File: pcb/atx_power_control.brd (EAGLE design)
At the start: 86 x 70 mm, 65 parts, among them IC2 REG1117, IC3 STM32F042F4, IC4 MY_7905DT, J1 ATX24RH, SW1 324_SW, SW2 324_SW, SW3 324_SW, SW4 324_SW, SW5 324_SW, SW7 324_SW, U1 USBC_16P, U2 USBC_16P

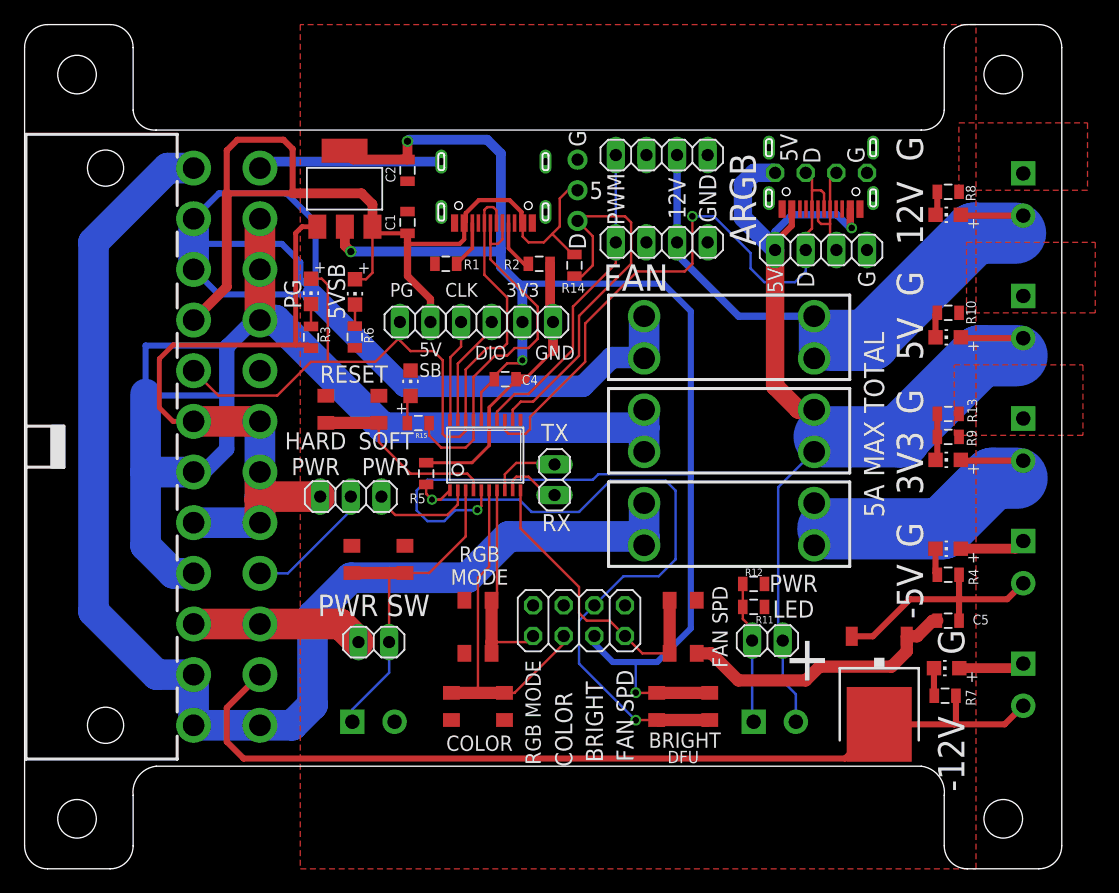
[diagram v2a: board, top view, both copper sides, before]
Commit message: adjusted LED resistor value, optimised GND plane
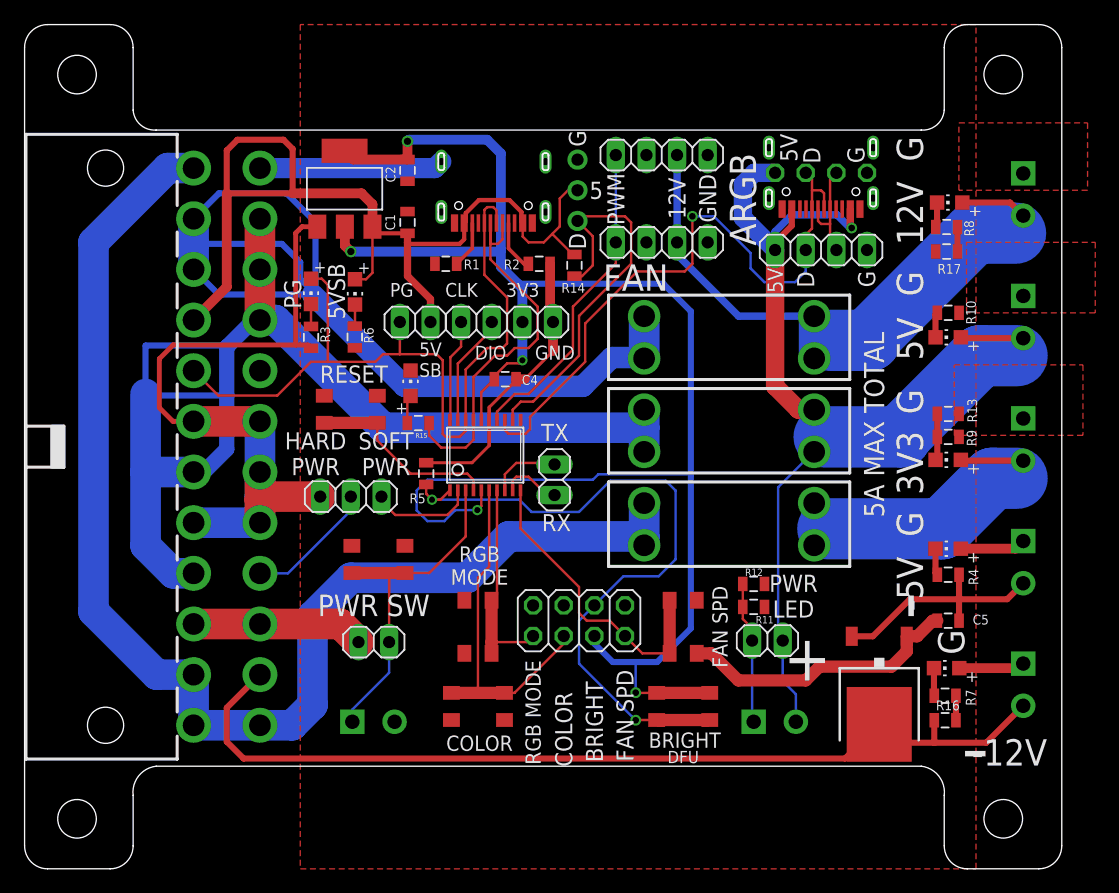
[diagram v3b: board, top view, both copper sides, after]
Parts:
- added R16, R17: 5K, SparkFun-Passives:0805
- moved R8 2.92 mm to (76.5, 53.2)
- moved LED5 1.02 mm to (76.7, 55.2)
- moved SW3 0.13 mm to (27.1, 38.1)
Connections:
- new net N$28: R16.2, R7.1
- new net N$32: R17.2, R8.1
- net GND: now also R17.1; no longer R8.1
- net N$2: now also R16.1; no longer R7.1
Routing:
- net N$32: track 0.00 -> 2.03 mm
- net N$28: track 0.00 -> 2.03 mm
- net N$2: track 77.6 -> 78.3 mm
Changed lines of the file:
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@@
 <board>
 <plain>
-<text x="73.406" y="22.987" size="2.1844" layer="25" rot="R90" align="center">-5V</text>
+<text x="73.406" y="23.622" size="2.1844" layer="25" rot="R90" align="center">-5V</text>
 <text x="73.406" y="33.655" size="2.1844" layer="25" rot="R90" align="center">3V3</text>
-<text x="76.835" y="9.525" size="2.1844" layer="25" rot="R90" align="center">-12V</text>
+<text x="81.661" y="9.652" size="2.1844" layer="25" rot="R180" align="center">-12V</text>
 <text x="73.406" y="43.942" size="2.1844" layer="25" rot="R90" align="center">5V</text>
 <text x="73.406" y="54.356" size="2.1844" layer="25" rot="R90" align="center">12V</text>
@@
 <text x="73.406" y="48.514" size="2.1844" layer="25" rot="R270" align="center">G</text>
 <text x="73.406" y="38.735" size="2.1844" layer="25" rot="R270" align="center">G</text>
-<text x="73.406" y="27.686" size="2.1844" layer="25" rot="R270" align="center">G</text>
+<text x="73.406" y="28.575" size="2.1844" layer="25" rot="R270" align="center">G</text>
 <text x="76.835" y="18.796" size="2.1844" layer="25" rot="R270" align="center">G</text>
 <text x="33.655" y="42.2102" size="1.143" layer="25" rot="R180" align="center">5V
@@
 <text x="45.8424" y="52.0408" size="1.4224" layer="25" rot="R270" align="center">D</text>
 <text x="47.4002" y="56.2564" size="1.4224" layer="25" align="center">5</text>
+<rectangle x1="77.978" y1="9.3218" x2="79.6798" y2="9.779" layer="25"/>
+<rectangle x1="72.6567" y1="21.5773" x2="74.3585" y2="22.0345" layer="25" rot="R90"/>
 </plain>
 <attributes>
@@
 <attribute name="NAME" x="42.5706" y="40.9413" size="0.8128" layer="25" rot="R180"/>
 </element>
-<element name="SW3" library="3pos_slide_switch_centered" package="342_SWICH_FOOT" value="324_SW" x="27.178" y="38.1" smashed="yes" rot="R180"/>
+<element name="SW3" library="3pos_slide_switch_centered" package="342_SWICH_FOOT" value="324_SW" x="27.051" y="38.1" smashed="yes" rot="R180"/>
 <element name="SW4" library="3pos_slide_switch_centered" package="342_SWICH_FOOT" value="324_SW" x="54.61" y="13.462" smashed="yes" rot="R180"/>
 <element name="LED1" library="adafruit" package="CHIP-LED0805" value="" x="76.581" y="26.543" smashed="yes" rot="R90">
@@
 <attribute name="NAME" x="78.0415" y="14.859" size="0.8128" layer="25" rot="R270"/>
 </element>
-<element name="LED5" library="adafruit" package="CHIP-LED0805" value="" x="76.581" y="54.229" smashed="yes" rot="R90">
-<attribute name="VALUE" x="77.851" y="56.769" size="1.27" layer="27" rot="R180"/>
-</element>
-<element name="R8" library="SparkFun-Passives" package="0805" value="5K" x="76.581" y="56.134" smashed="yes" rot="R180">
-<attribute name="NAME" x="78.0415" y="56.6928" size="0.8128" layer="25" rot="R270"/>
+<element name="LED5" library="adafruit" package="CHIP-LED0805" value="" x="76.708" y="55.245" smashed="yes" rot="R90">
+<attribute name="VALUE" x="77.978" y="57.785" size="1.27" layer="27" rot="R180"/>
+</element>
+<element name="R8" library="SparkFun-Passives" package="0805" value="5K" x="76.454" y="53.213" smashed="yes" rot="R180">
+<attribute name="NAME" x="77.9145" y="53.7718" size="0.8128" layer="25" rot="R270"/>
 </element>
 <element name="LED6" library="adafruit" package="CHIP-LED0805" value="" x="76.581" y="33.909" smashed="yes" rot="R90">
@@
 <element name="LED8" library="adafruit" package="CHIP-LED0805" value="" x="32.004" y="40.259" smashed="yes">
 <attribute name="VALUE" x="34.544" y="38.989" size="1.27" layer="27" rot="R90"/>
+</element>
+<element name="R16" library="SparkFun-Passives" package="0805" value="5K" x="76.327" y="12.319" smashed="yes">
+<attribute name="NAME" x="75.565" y="13.1445" size="0.8128" layer="25"/>
+</element>
+<element name="R17" library="SparkFun-Passives" package="0805" value="5K" x="76.454" y="51.181" smashed="yes">
+<attribute name="NAME" x="75.692" y="49.3395" size="0.8128" layer="25"/>
 </element>
 </elements>
@@
 <contactref element="LED1" pad="A"/>
 <contactref element="LED4" pad="A"/>
-<contactref element="R8" pad="1"/>
 <contactref element="R9" pad="1"/>
 <contactref element="R10" pad="1"/>
@@
 <contactref element="JP2" pad="4"/>
 <contactref element="JP7" pad="4"/>
-<wire x1="34.556" y1="58.6395" x2="20.0535" y2="58.6395" width="0.8128" layer="16"/>
-<wire x1="20.0535" y1="58.6395" x2="19.514" y2="58.1" width="0.8128" layer="16"/>
 <contactref element="JP6" pad="1"/>
 <contactref element="J5" pad="2"/>
@@
 <contactref element="JP11" pad="3"/>
 <contactref element="LED8" pad="C"/>
+<contactref element="R17" pad="1"/>
+<wire x1="34.556" y1="58.6395" x2="34.0165" y2="58.1" width="1.6764" layer="16"/>
+<wire x1="34.0165" y1="58.1" x2="19.514" y2="58.1" width="1.6764" layer="16"/>
 </signal>
 <signal name="+3V3">
@@
 <wire x1="37.221" y1="32.248" x2="37.221" y2="31.3862" width="0.2032" layer="1"/>
 <wire x1="37.221" y1="32.248" x2="36.703" y2="32.766" width="0.2032" layer="1"/>
-<wire x1="29.378" y1="36.975" x2="24.978" y2="36.975" width="1.016" layer="1"/>
+<wire x1="29.251" y1="36.975" x2="24.851" y2="36.975" width="1.016" layer="1"/>
 <wire x1="36.703" y1="32.766" x2="32.004" y2="32.766" width="0.2032" layer="1"/>
-<wire x1="29.378" y1="36.975" x2="29.378" y2="35.392" width="0.2032" layer="1"/>
-<wire x1="29.378" y1="35.392" x2="32.004" y2="32.766" width="0.2032" layer="1"/>
+<wire x1="29.251" y1="36.975" x2="29.251" y2="35.519" width="0.2032" layer="1"/>
+<wire x1="29.251" y1="35.519" x2="32.004" y2="32.766" width="0.2032" layer="1"/>
 </signal>
 <signal name="BUTTON2">
@@
 <contactref element="IC4" pad="3"/>
 <contactref element="J1" pad="14"/>
-<contactref element="R7" pad="1"/>
 <contactref element="J3" pad="2"/>
 <wire x1="68.032" y1="9.144" x2="70.866" y2="11.978" width="0.508" layer="1"/>
@@
 <wire x1="16.764" y1="10.541" x2="18.161" y2="9.144" width="0.508" layer="1"/>
 <wire x1="18.161" y1="9.144" x2="68.032" y2="9.144" width="0.508" layer="1"/>
-<wire x1="70.866" y1="11.978" x2="77.089" y2="11.978" width="0.508" layer="1"/>
-<wire x1="77.089" y1="11.978" x2="81.264" y2="11.978" width="0.508" layer="1"/>
-<wire x1="81.264" y1="11.978" x2="82.804" y2="13.518" width="0.508" layer="1"/>
-<wire x1="77.227" y1="14.351" x2="77.227" y2="12.116" width="0.508" layer="1"/>
-<wire x1="77.227" y1="12.116" x2="77.089" y2="11.978" width="0.508" layer="1"/>
+<wire x1="79.74" y1="10.454" x2="75.438" y2="10.454" width="0.508" layer="1"/>
+<wire x1="75.438" y1="10.454" x2="72.39" y2="10.454" width="0.508" layer="1"/>
+<wire x1="70.866" y1="11.978" x2="72.39" y2="10.454" width="0.508" layer="1"/>
+<wire x1="79.74" y1="10.454" x2="82.804" y2="13.518" width="0.508" layer="1"/>
+<contactref element="R16" pad="1"/>
+<wire x1="75.427" y1="12.319" x2="75.427" y2="10.465" width="0.508" layer="1"/>
+<wire x1="75.427" y1="10.465" x2="75.438" y2="10.454" width="0.508" layer="1"/>
 </signal>
 <signal name="N$11">
@@
 <contactref element="LED5" pad="C"/>
 <contactref element="R8" pad="2"/>
-<wire x1="75.681" y1="56.134" x2="75.681" y2="54.379" width="0.508" layer="1"/>
-<wire x1="75.681" y1="54.379" x2="75.531" y2="54.229" width="0.508" layer="1"/>
+<wire x1="75.658" y1="55.245" x2="75.658" y2="53.317" width="0.508" layer="1"/>
+<wire x1="75.658" y1="53.317" x2="75.554" y2="53.213" width="0.508" layer="1"/>
 </signal>
 <signal name="N$10">
@@
 <wire x1="23.749" y1="42.037" x2="20.955" y2="39.243" width="0.2032" layer="1"/>
 <wire x1="25.146" y1="42.037" x2="23.749" y2="42.037" width="0.2032" layer="1"/>
-<wire x1="31.115" y1="44.069" x2="29.083" y2="42.037" width="0.2032" layer="1"/>
-<wire x1="29.083" y1="42.037" x2="25.146" y2="42.037" width="0.2032" layer="1"/>
+<wire x1="25.146" y1="42.037" x2="29.083" y2="42.037" width="0.2032" layer="1"/>
 <wire x1="34.925" y1="35.814" x2="34.671" y2="36.068" width="0.2032" layer="1"/>
-<wire x1="34.671" y1="42.164" x2="33.909" y2="42.926" width="0.2032" layer="1"/>
-<wire x1="33.909" y1="42.926" x2="32.004" y2="42.926" width="0.2032" layer="1"/>
-<wire x1="31.115" y1="43.815" x2="31.115" y2="45.339" width="0.2032" layer="1"/>
+<wire x1="34.163" y1="42.672" x2="34.671" y2="42.164" width="0.2032" layer="1"/>
 <wire x1="34.671" y1="36.068" x2="34.671" y2="42.164" width="0.2032" layer="1"/>
-<wire x1="32.004" y1="42.926" x2="31.115" y2="43.815" width="0.2032" layer="1"/>
-<wire x1="31.115" y1="44.069" x2="31.115" y2="45.339" width="0" layer="19" extent="1-1"/>
+<wire x1="29.083" y1="42.037" x2="29.718" y2="42.672" width="0.2032" layer="1"/>
+<wire x1="29.718" y1="42.672" x2="31.115" y2="42.672" width="0.2032" layer="1"/>
+<wire x1="31.115" y1="42.672" x2="34.163" y2="42.672" width="0.2032" layer="1"/>
+<wire x1="31.115" y1="45.339" x2="31.115" y2="42.672" width="0.2032" layer="1"/>
 </signal>
 <signal name="N$30">
@@
 <contactref element="U$5" pad="B0"/>
 <contactref element="U$5" pad="B1"/>
-<wire x1="82.804" y1="54.158" x2="77.702" y2="54.158" width="0.508" layer="1"/>
-<wire x1="77.702" y1="54.158" x2="77.631" y2="54.229" width="0.508" layer="1"/>
 <wire x1="82.169" y1="52.705" x2="78.74" y2="52.705" width="5.08" layer="16"/>
 <wire x1="78.74" y1="52.705" x2="70.104" y2="44.069" width="5.08" layer="16"/>
@@
 <wire x1="66.802" y1="43.701" x2="66.802" y2="43.651" width="0.2032" layer="16"/>
 <wire x1="66.802" y1="43.651" x2="65.47" y2="42.319" width="0.2032" layer="16"/>
+<wire x1="77.758" y1="55.245" x2="81.717" y2="55.245" width="0.508" layer="1"/>
+<wire x1="81.717" y1="55.245" x2="82.804" y2="54.158" width="0.508" layer="1"/>
 </signal>
 <signal name="N$16">
@@
 <wire x1="31.739" y1="38.944" x2="31.739" y2="36.957" width="0.2032" layer="1"/>
 </signal>
+<signal name="N$28">
+<contactref element="R7" pad="1"/>
+<contactref element="R16" pad="2"/>
+<wire x1="77.227" y1="14.351" x2="77.227" y2="12.319" width="0.508" layer="1"/>
+</signal>
+<signal name="N$32">
+<contactref element="R8" pad="1"/>
+<contactref element="R17" pad="2"/>
+<wire x1="77.354" y1="53.213" x2="77.354" y2="51.181" width="0.508" layer="1"/>
+</signal>
 </signals>

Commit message: moved ARGB header, removed GND thermals, jumper pad on USBC data lines, finishing touches
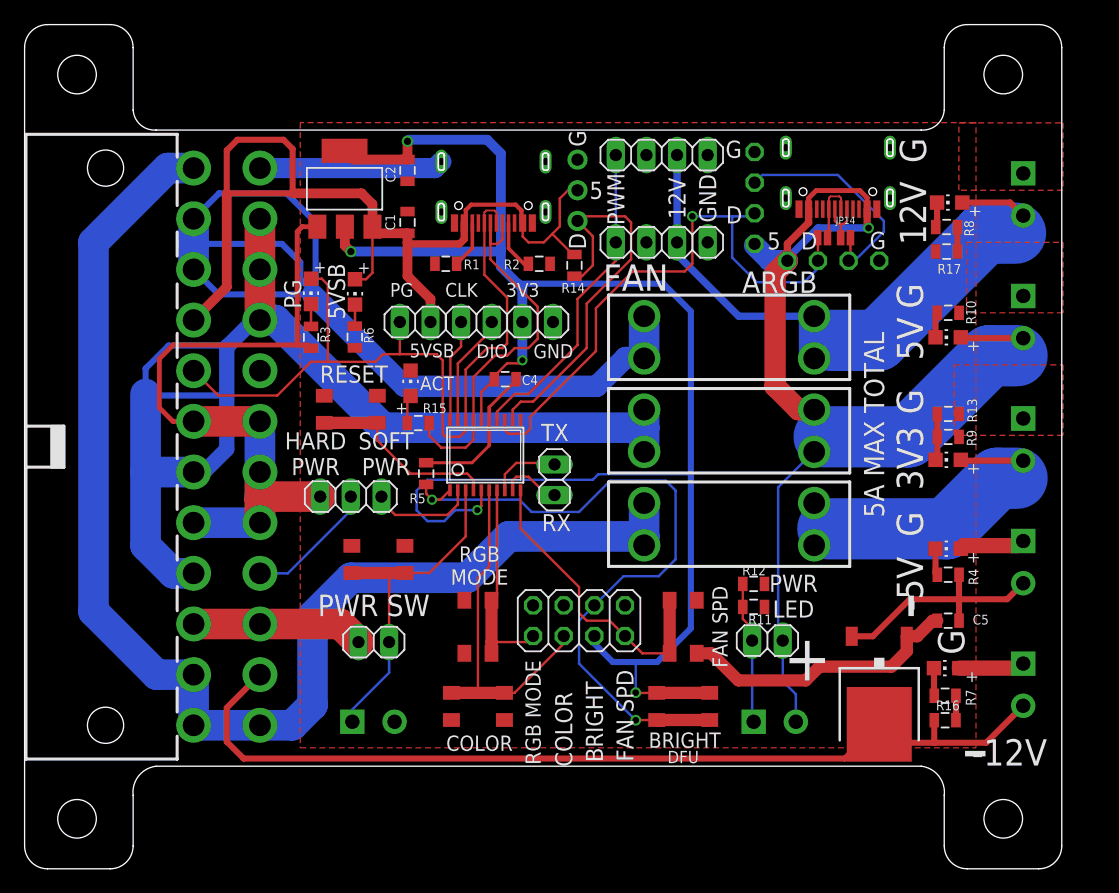
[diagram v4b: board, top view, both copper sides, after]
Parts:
- added JP13, JP14: JUMPER-SMT_2_NO_NO-SILK, SparkFun-Jumpers:SMT-JUMPER_2_NO_NO-SILK
- C1, C4: value 1uF -> 100nF; device clock:0805@1 -> atx_power_control:0805$1
- C2, C5: value 1uF -> 10uF; device clock:0805@1 -> atx_power_control:0805$1
- IC2: device clock:SOT223 -> atx_power_control:SOT223
- JP11: device adafruit_changed:1X03-CLEANBIG -> atx_power_control:1X03-CLEANBIG
- JP12: device adafruit_changed:1X06 -> atx_power_control:1X06
- JP2, JP4, JP8: device pinhead:1X04 -> atx_power_control:1X04
- JP5: device pinhead:1X03 -> atx_power_control:1X03
- JP6: device pinhead:1X02 -> atx_power_control:1X02
- JP7: device pinhead:1X04 -> atx_power_control:1X06
- JP9: device pinhead:2X04 -> atx_power_control:2X04
- R1, R2, R5: value 5.1K -> 5K1; device joyAnalog:0805 -> atx_power_control:0805
- R10, R11, R12, R13, R3, R6, R9: value 1K -> 5K1; device SparkFun-Passives:0805 -> atx_power_control:0805
- R14, R15: value 5k1 -> 5K1; device SparkFun-Passives:0805 -> atx_power_control:0805
- R16, R7: value 5K -> 5K1
- R17, R8: value 5K -> 5K1; device SparkFun-Passives:0805 -> atx_power_control:0805
- R4: value 1K -> 5K1
- moved JP12 8.06 mm to (60.5, 58.2), turned to 90 degrees
- moved JP7 3.67 mm to (69.6, 50.4)
- moved U1 1.40 mm to (67.4, 58.5)
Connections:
- new net N$34: JP13.2, U1.A6, U1.B6
- new net N$37: JP12.3, JP14.2, JP7.3
- net N$35: now also JP13.1; no longer U1.A6, U1.B6
- net N$36: now also JP14.1; no longer JP12.3, JP7.3
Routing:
- net N$37: track 0.00 -> 19.3 mm
- net GND: track 153.2 -> 141.8 mm
- net N$34: track 0.00 -> 5.39 mm
- net N$36: track 8.92 -> 4.34 mm
- net N$35: track 52.6 -> 48.6 mm
- net N$10: track 102.3 -> 101.2 mm
- net N$30: track 94.5 -> 95.0 mm
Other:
- board text added: "ACT"
- board text removed: "5V SB"

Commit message: wired to softpower by default
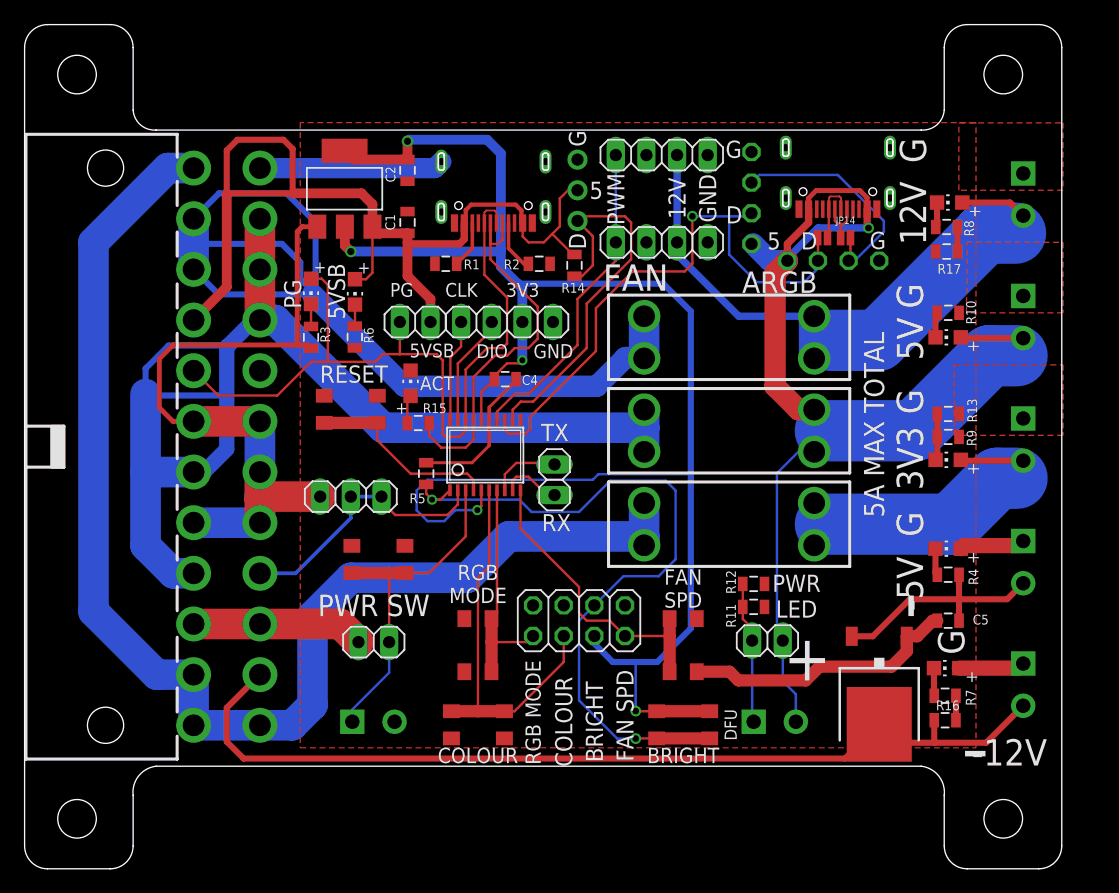
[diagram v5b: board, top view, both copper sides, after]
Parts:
- moved SW2 1.52 mm to (37.6, 11.9)
- moved SW4 1.52 mm to (54.6, 11.9)
- moved SW5 1.52 mm to (37.6, 18.5)
- moved SW7 1.52 mm to (54.6, 18.5)
- moved JP12 0.25 mm to (60.3, 58.2)
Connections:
- removed net N$24: IC3.2, JP5.1
- net N$25: now also IC3.2, JP5.1
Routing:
- net N$25: track 10.8 -> 22.5 mm
- net N$24: track 8.72 -> 0.00 mm
- net N$13: track 28.8 -> 31.9 mm
- net BUTTON2: track 57.5 -> 59.9 mm
- net N$22: track 17.4 -> 18.9 mm
- net +3V3: track 148.2 -> 149.7 mm
- net N$30: track 95.0 -> 96.3 mm
- net GND: track 141.8 -> 141.2 mm
- net N$27: track 25.5 -> 24.9 mm
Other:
- board text added: "ATX4VC.com dekuNukem OCT 2022 PD1"
- board text added: "COLOUR"
- board text removed: "ATX4VC.com dekuNukem SEPT 2022 PD1"
- board text removed: "COLOR"

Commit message: pretty much done
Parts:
- moved R12 2.50 mm to (62.7, 22.6), turned to 90 degrees
- moved C5 2.03 mm to (76.6, 22.6)
- moved R11 0.97 mm to (60.8, 22.6), turned to 90 degrees
- moved JP12 0.13 mm to (60.4, 58.2)
- moved R4 0.13 mm to (76.6, 24.5)
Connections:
- net GND: now also J8.1, JP1.2; no longer R11.1, R12.1
- net N$17: now also J8.2, JP1.1, R11.1, R12.1; no longer J8.1, JP1.2, R11.2, R12.2
- net N$30: now also R11.2, R12.2; no longer J8.2, JP1.1
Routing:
- net GND: track 141.2 -> 151.7 mm
- net N$30: track 96.3 -> 86.2 mm
- net N$11: track 19.9 -> 18.3 mm
- net N$25: track 22.5 -> 21.7 mm
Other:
- board text added: "MAX 5A TOTAL"
- board text removed: "5A MAX TOTAL"
